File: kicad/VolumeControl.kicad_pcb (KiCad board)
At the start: 2 copper layers, 47 parts, among them P1 PWR_IN, P2 SOURCE_1, P3 SOURCE_2, P4 CONTROL, P5 AUDIO_OUT, P6 PWR_OUT, U1 ILQ74, U2 7805, U3 TMR_3-1221, U4 OPA1664, U5 PGA4311, U6 OPA1664

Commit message: Adding untracked files
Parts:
- removed C10, C11: 0.1u, Capacitors_SMD:C_1206_HandSoldering
- removed the REF** at (87.6, 124.5)
- removed the REF** at (87.6, 88.9)
- removed the REF** at (166.4, 88.9)
- removed the REF** at (166.4, 124.5)
- removed U6: OPA1664, SMD_Packages:SOIC-14_N
- added P7: AUDIO_OUT, JST:JST-4RA, F.Cu at (184.2, 87.6)
- added REF**: MountingHole_3.2mm_M3, Mounting_Holes:MountingHole_3.2mm_M3, F.Cu at (106.7, 86.4)
- added REF**: MountingHole_3.2mm_M3, Mounting_Holes:MountingHole_3.2mm_M3, F.Cu at (106.6, 123.3)
- added REF**: MountingHole_3.2mm_M3, Mounting_Holes:MountingHole_3.2mm_M3, F.Cu at (196.6, 123.3)
- added REF**: MountingHole_3.2mm_M3, Mounting_Holes:MountingHole_3.2mm_M3, F.Cu at (196.6, 86.3)
- C2: value 0.33u -> 0.1u
- C5: value 0.1u -> 1u
- C7: value 1u -> 0.1u
- P1: footprint Pin_Headers:Pin_Header_Straight_1x02 -> JST:JST-3RA
- P2: value SOURCE_1 -> PWR_OUT; footprint Pin_Headers:Pin_Header_Straight_1x04 -> JST:JST-2RA
- P3: value SOURCE_2 -> SOURCE_1; footprint Pin_Headers:Pin_Header_Straight_1x04 -> JST:JST-4RA
- P4: value CONTROL -> SOURCE_2; footprint Pin_Headers:Pin_Header_Straight_1x05 -> JST:JST-4RA
- P5: value AUDIO_OUT -> CONTROL; footprint Pin_Headers:Pin_Header_Straight_1x04 -> JST:JST-5RA
- P6: value PWR_OUT -> AUDIO_OUT; footprint Pin_Headers:Pin_Header_Straight_1x02 -> JST:JST-4RA
- U2: value 7805 -> TMR_3-1221; footprint Power_Integrations:TO-220 -> TracoPower:TMR_3
- U3: value TMR_3-1221 -> OPA1664; footprint TracoPower:TMR_3 -> SMD_Packages:SOIC-14_N
- U4: value OPA1664 -> PGA4311; footprint SMD_Packages:SOIC-14_N -> SMD_Packages:SOIC-28
- U5: value PGA4311 -> OPA1664; footprint SMD_Packages:SOIC-28 -> SMD_Packages:SOIC-14_N
- moved P6 96.7 mm to (184.2, 121.9)
- moved P4 84.2 mm to (170.2, 121.9), turned to 0 degrees
- moved C7 76.9 mm to (191.1, 108.6)
- moved C3 69.3 mm to (158.1, 87.6), turned to 180 degrees
- moved R13 58.5 mm to (172.7, 94.6), turned to 270 degrees
- moved U5 52.6 mm to (184.3, 109.2), turned to 270 degrees
- moved C4 49.6 mm to (165.7, 87.6), turned to 180 degrees
- moved P5 48.7 mm to (119.4, 121.9)
- moved R11 48.4 mm to (167.6, 116.8), turned to 0 degrees
- moved U3 44.1 mm to (163.2, 109.2), turned to 270 degrees
- moved C6 42.7 mm to (177.2, 108.6), turned to 90 degrees
- moved R12 41.9 mm to (172.7, 116.8)
- moved P3 40.9 mm to (156.2, 121.9), turned to 0 degrees
- moved R9 40.9 mm to (153.7, 116.8)
- moved U2 40.9 mm to (133.3, 102.2), turned to 0 degrees
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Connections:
- C2 pad 1: +12V -> +5VD
- C3 pad 1: +5VD -> +5VA
- C3 pad 2: GNDD -> GNDA
- C4 pad 1: +5VD -> GNDA
- C4 pad 2: GNDD -> -5VA
- C5 pad 1: +5VA -> +5VD
- C5 pad 2: GNDA -> GNDD
- C6 pad 1: GNDA -> +5VA
- C6 pad 2: -5VA -> GNDA
- C7 pad 1: +5VD -> GNDA
- C7 pad 2: GNDD -> -5VA
- P1 pad 1: +12V -> +5VD
- P1 pad 2: GNDD -> +12V
- P2 pad 1: /Audio Processing/SOURCE_1_LEFT -> +5VD
- P2 pad 2: GNDA -> GNDD
- P3 pad 1: /Audio Processing/SOURCE_2_LEFT -> /Audio Processing/SOURCE_1_LEFT
- P3 pad 2: GNDA -> GNDD
- P3 pad 3: GNDA -> GNDD
- P3 pad 4: /Audio Processing/SOURCE_2_RIGHT -> /Audio Processing/SOURCE_1_RIGHT
- P4 pad 1: /Digital Control/MUTE -> /Audio Processing/SOURCE_2_LEFT
- P4 pad 2: /Digital Control/CS -> GNDD
- P4 pad 3: /Digital Control/SDA -> GNDD
- P4 pad 4: /Digital Control/SCL -> /Audio Processing/SOURCE_2_RIGHT
- P5 pad 1: /Audio Processing/LEFT -> /Digital Control/MUTE
- P5 pad 2: GNDA -> /Digital Control/CS
- P5 pad 3: GNDA -> /Digital Control/SDA
- P5 pad 4: /Audio Processing/RIGHT -> /Digital Control/SCL
- P6 pad 1: +5VD -> /Audio Processing/LEFT
- P6 pad 2: GNDD -> GNDA
- R1 pad 2: /Digital Control/SCL -> /Digital Control/MUTE
- R10 pad 1: /Audio Processing/SOURCE_2_LEFT -> /Audio Processing/SOURCE_1_RIGHT
- R10 pad 2: GNDA -> GNDD
- R11 pad 1: /Audio Processing/SOURCE_1_RIGHT -> /Audio Processing/SOURCE_2_LEFT
- R11 pad 2: GNDA -> GNDD
- R12 pad 2: GNDA -> GNDD
- R2 pad 2: /Digital Control/SDA -> /Digital Control/CS
- R3 pad 2: /Digital Control/CS -> /Digital Control/SDA
- R4 pad 2: /Digital Control/MUTE -> /Digital Control/SCL
- R5 pad 1: /Audio Processing/SCL_ISOLATED -> /Audio Processing/MUTE_ISOLATED
- R6 pad 1: /Audio Processing/SDA_ISOLATED -> /Audio Processing/CS_ISOLATED
- R7 pad 1: /Audio Processing/CS_ISOLATED -> /Audio Processing/SDA_ISOLATED
- R8 pad 1: /Audio Processing/MUTE_ISOLATED -> /Audio Processing/SCL_ISOLATED
- R9 pad 2: GNDA -> GNDD
- U1 pad 10: /Audio Processing/MUTE_ISOLATED -> /Audio Processing/SCL_ISOLATED
- U1 pad 11: /Audio Processing/CS_ISOLATED -> /Audio Processing/SDA_ISOLATED
- U1 pad 14: /Audio Processing/SDA_ISOLATED -> /Audio Processing/CS_ISOLATED
- U1 pad 15: /Audio Processing/SCL_ISOLATED -> /Audio Processing/MUTE_ISOLATED
- U2 pad 1: +12V -> GNDD
- U2 pad 2: GNDD -> Net-(L1-Pad2)
- U2 pad 3: +5VD -> Net-(U2-Pad3)
- U3 pad 1: GNDD -> Net-(U3-Pad1)
- U3 pad 2: Net-(L1-Pad2) -> Net-(U3-Pad1)
- U3 pad 3: Net-(U3-Pad3) -> /Audio Processing/SOURCE_1_LEFT
- U3 pad 5: Net-(U3-Pad5) -> /Audio Processing/SOURCE_1_RIGHT
- U3 pad 6: +5VA -> Net-(U3-Pad6)
- U3 pad 7: GNDA -> Net-(U3-Pad6)
- U3 pad 8: -5VA -> Net-(U3-Pad8)
- U4 pad 1: Net-(U4-Pad1) -> /Audio Processing/MUTE_ISOLATED
- U4 pad 10: /Audio Processing/SOURCE_1_RIGHT -> Net-(U3-Pad1)
- U4 pad 11: -5VA -> GNDA
- U4 pad 12: /Audio Processing/SOURCE_2_RIGHT -> +5VD
- U4 pad 13: Net-(U4-Pad13) -> /Audio Processing/SDA_ISOLATED
- U4 pad 14: Net-(U4-Pad13) -> /Audio Processing/CS_ISOLATED
- U4 pad 2: Net-(U4-Pad1) -> GNDA
- U4 pad 3: /Audio Processing/SOURCE_1_LEFT -> Net-(U3-Pad8)
- U4 pad 4: +5VA -> GNDA
- U4 pad 5: /Audio Processing/SOURCE_2_LEFT -> Net-(R14-Pad2)
- U4 pad 6: Net-(U4-Pad6) -> -5VA
- U4 pad 7: Net-(U4-Pad6) -> +5VA
- U4 pad 8: Net-(U4-Pad8) -> Net-(R15-Pad2)
- U4 pad 9: Net-(U4-Pad8) -> GNDA
- U5 pad 1: /Audio Processing/MUTE_ISOLATED -> /Audio Processing/LEFT
- U5 pad 10: Net-(U4-Pad8) -> (no net)
- U5 pad 11: GNDA -> -5VA
- U5 pad 12: +5VD -> GNDA
- U5 pad 13: /Audio Processing/SDA_ISOLATED -> Net-(R16-Pad1)
- U5 pad 14: /Audio Processing/CS_ISOLATED -> /Audio Processing/RIGHT
- U5 pad 2: GNDA -> Net-(R14-Pad1)
- U5 pad 3: Net-(U4-Pad1) -> GNDA
- U5 pad 4: GNDA -> +5VA
- U5 pad 5: Net-(R14-Pad2) -> (no net)
- U5 pad 6: -5VA -> (no net)
- U5 pad 7: +5VA -> (no net)
- U5 pad 8: Net-(R16-Pad2) -> (no net)
- U5 pad 9: GNDA -> (no net)
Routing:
- net GNDA: track 0.00 -> 84.9 mm, vias 0 -> 2
- net /Audio Processing/MUTE_ISOLATED: track 0.00 -> 78.8 mm, vias 0 -> 2
- net +5VD: track 0.00 -> 61.5 mm, vias 0 -> 2
- net /Audio Processing/CS_ISOLATED: track 0.00 -> 51.2 mm, vias 0 -> 1
- net /Audio Processing/SDA_ISOLATED: track 0.00 -> 45.3 mm, vias 0 -> 1
- net GNDD: track 0.00 -> 43.7 mm, vias 0 -> 1
- net /Audio Processing/RIGHT: track 0.00 -> 41.1 mm
- net /Audio Processing/LEFT: track 0.00 -> 39.8 mm, vias 0 -> 2
- net +5VA: track 0.00 -> 39.8 mm, vias 0 -> 2
- net /Audio Processing/SCL_ISOLATED: track 0.00 -> 38.1 mm, vias 0 -> 1
- net Net-(R17-Pad2): track 0.00 -> 30.4 mm, vias 0 -> 2
- net /Digital Control/CTRL_GND: track 0.00 -> 29.2 mm
- net Net-(R15-Pad2): track 0.00 -> 26.8 mm, vias 0 -> 5
- net Net-(R16-Pad2): track 0.00 -> 25.4 mm, vias 0 -> 2
- net Net-(U3-Pad8): track 0.00 -> 24.7 mm, vias 0 -> 2
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- added copper zone on In2.Cu, net +5VA
- added copper zone on In2.Cu, net +5VD
- added copper zone on In2.Cu, net -5VA
- added copper zone on In1.Cu, net GNDA
- added copper zone on In1.Cu, net GNDD
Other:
- board outline added: 100 x 47 mm
- copper layers 2 -> 4
- net class Default: trace_width 0.25 -> 0.5
- net class Power added: clearance 0.2, trace_width 1, via_dia 1, via_drill 0.6
- rule pad_to_mask_clearance: 0.2 -> 0
- board text added: "5V OUT"
- board text added: "AUDIO_OUT"
- board text added: "CONTROL"
- board text added: "POWER"
- board text added: "SOURCE_1"
- board text added: "SOURCE_2"
- board text added: "Volume Control V1.0"
- board text added: "v@nce.me"

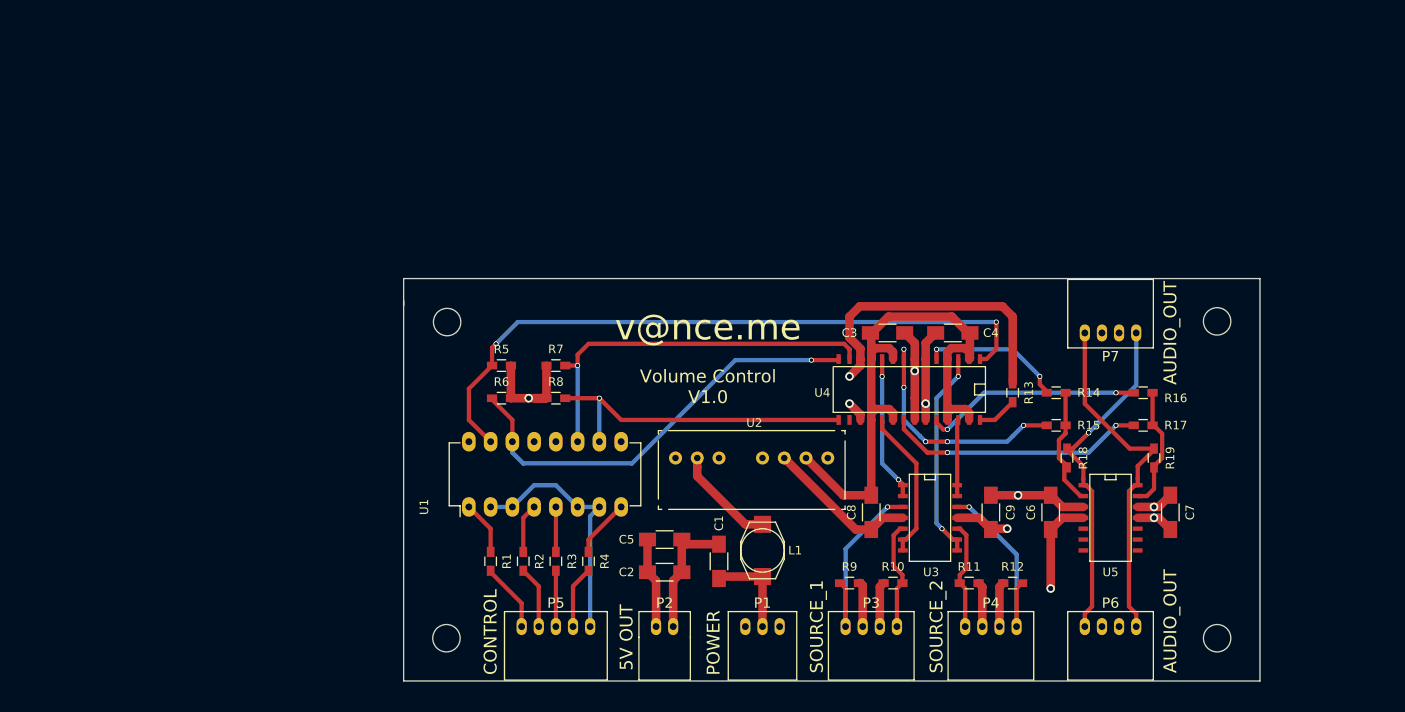
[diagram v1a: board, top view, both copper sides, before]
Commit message: Routed the board.  Passes ERC check
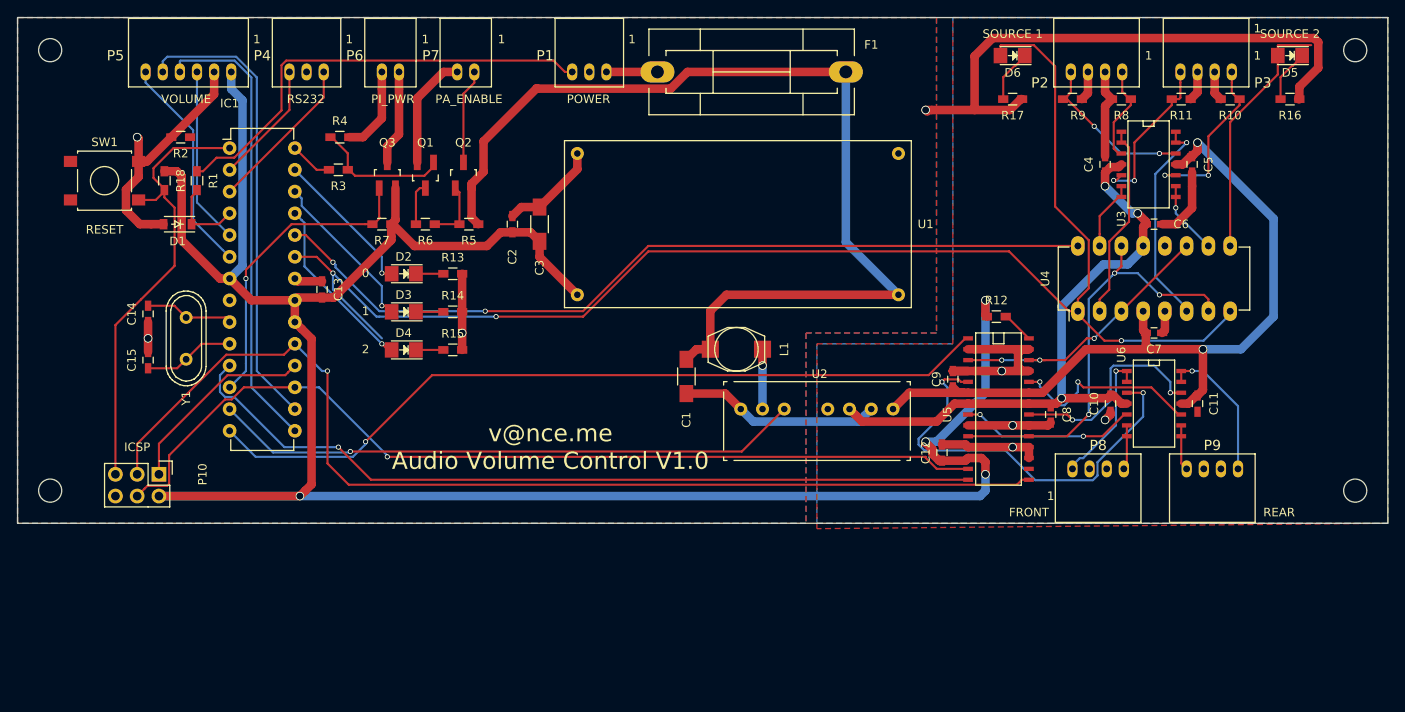
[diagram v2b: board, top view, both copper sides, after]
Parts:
- removed R19: 47k, Resistors_SMD:R_0603_HandSoldering
- removed the REF** at (106.7, 86.4)
- removed the REF** at (106.6, 123.3)
- removed the REF** at (196.6, 123.3)
- removed the REF** at (196.6, 86.3)
- added C10: 0.1u, Capacitors_SMD:C_0603_HandSoldering, F.Cu at (184.2, 95.9)
- added C11: 0.1u, Capacitors_SMD:C_0603_HandSoldering, F.Cu at (194.3, 95.9)
- added C12: 0.1u, Capacitors_SMD:C_0603_HandSoldering, F.Cu at (164.5, 101.6)
- added C13: 0.1u, Capacitors_SMD:C_0603_HandSoldering, F.Cu at (92.1, 82.5)
- added C14: 22p, Capacitors_SMD:C_0603_HandSoldering, F.Cu at (71.8, 85.4)
- added C15: 22p, Capacitors_SMD:C_0603_HandSoldering, F.Cu at (71.8, 90.8)
- added D1: 5.1V, Diodes_SMD:SOD-123, F.Cu at (75.2, 74.9)
- added D2: 0, LEDs:LED_1206, F.Cu at (101.6, 80.7)
- added D3: 1, LEDs:LED_1206, F.Cu at (101.6, 85.2)
- added D4: 2, LEDs:LED_1206, F.Cu at (101.6, 89.6)
- added D5: S2, LEDs:LED_1206, F.Cu at (205.1, 55.2)
- added D6: S1, LEDs:LED_1206, F.Cu at (172.7, 55.2)
- added F1: 1A, Fuse_Holders_and_Fuses:Fuseholder5x20_horiz_SemiClosed_Casing10x25mm, F.Cu at (142.2, 57.1)
- added IC1: ATMEGA328P-P, Housings_DIP:DIP-28_W7.62mm, F.Cu at (81.3, 66.0)
- added P10: ICSP, Pin_Headers:Pin_Header_Straight_2x03, F.Cu at (73.0, 104.1)
- added P8: FRONT, JST:JST-4RA, F.Cu at (182.7, 103.5)
- added P9: REAR, JST:JST-4RA, F.Cu at (196.0, 103.5)
- added Q1: BC848B, TO_SOT_Packages_SMD:SOT-23_Handsoldering, F.Cu at (104.1, 69.2)
- added Q2: Si2301BDS, TO_SOT_Packages_SMD:SOT-23_Handsoldering, F.Cu at (108.6, 69.2)
- added Q3: Si2301BDS, TO_SOT_Packages_SMD:SOT-23_Handsoldering, F.Cu at (99.7, 69.2)
- added REF**: MountingHole_2.7mm_M2.5_ISO7380, Mounting_Holes:MountingHole_2.7mm_M2.5_ISO7380, F.Cu at (212.7, 54.6)
- added REF**: MountingHole_2.7mm_M2.5_ISO7380, Mounting_Holes:MountingHole_2.7mm_M2.5_ISO7380, F.Cu at (60.3, 54.6)
- added REF**: MountingHole_2.7mm_M2.5_ISO7380, Mounting_Holes:MountingHole_2.7mm_M2.5_ISO7380, F.Cu at (212.7, 106.0)
- added REF**: MountingHole_2.7mm_M2.5_ISO7380, Mounting_Holes:MountingHole_2.7mm_M2.5_ISO7380, F.Cu at (60.3, 106.0)
- added SW1: SW_PUSH, Buttons_Switches_SMD:SW_SPST_B3S-1000, F.Cu at (66.7, 69.8)
- added U6: OPA1664, SMD_Packages:SOIC-14_N, F.Cu at (189.4, 95.9)
- added Y1: 16MHz, Crystals:Crystal_HC49-U_Vertical, F.Cu at (76.2, 88.3)
- C2, C4, C6, C7, C8, C9: footprint Capacitors_SMD:C_1206_HandSoldering -> Capacitors_SMD:C_0603_HandSoldering
- C3: value 0.1u -> 1u
- C5: value 1u -> 0.1u; footprint Capacitors_SMD:C_1206_HandSoldering -> Capacitors_SMD:C_0603_HandSoldering
- P2: value PWR_OUT -> SOURCE_1; footprint JST:JST-2RA -> JST:JST-4RA
- P3: value SOURCE_1 -> SOURCE_2
- P4: value SOURCE_2 -> RS232; footprint JST:JST-4RA -> JST:JST-3RA
- P5: value CONTROL -> VOL_KNOB; footprint JST:JST-5RA -> JST:JST-6RA
- P6: value AUDIO_OUT -> PI_PWR; footprint JST:JST-4RA -> JST:JST-2RA
- P7: value AUDIO_OUT -> PA_EN; footprint JST:JST-4RA -> JST:JST-2RA
- R1, R3, R4: value 200 -> 10k
- R13, R14, R15, R16, R17: value 47k -> 220
- R18, R5, R7: value 47k -> 10k
- R2: value 200 -> 22k
- R6: value 47k -> 22k
- U1: value ILQ74 -> Buck_Converter; footprint Housings_DIP:DIP-16_W7.62mm_LongPads -> Buck_Converter:Buck_Converter
- U4: value PGA4311 -> DG308; footprint SMD_Packages:SOIC-28 -> Housings_DIP:DIP-16_W7.62mm_LongPads
- U5: value OPA1664 -> PGA4311; footprint SMD_Packages:SOIC-14_N -> SMD_Packages:SOIC-28
- moved R18 110.3 mm to (73.7, 69.8)
- moved P6 106.1 mm to (100.1, 57.1), turned to 180 degrees
- moved P4 102.9 mm to (90.3, 57.1), turned to 180 degrees
- moved P2 82.1 mm to (182.5, 57.1), turned to 180 degrees
- moved P7 81.2 mm to (108.9, 57.1)
- moved P5 77.7 mm to (76.5, 57.1), turned to 180 degrees
- moved P3 75.7 mm to (195.3, 57.1), turned to 180 degrees
- moved C5 75.6 mm to (193.7, 67.9), turned to 90 degrees
- moved R8 74.7 mm to (185.4, 60.3)
- moved R14 71.1 mm to (107.3, 85.2), turned to 0 degrees
- moved R15 71.0 mm to (107.3, 89.6), turned to 0 degrees
- moved R10 68.9 mm to (198.1, 60.3)
- moved P1 67.9 mm to (123.3, 57.1), turned to 180 degrees
- moved R13 66.8 mm to (107.3, 80.7), turned to 0 degrees
- moved R2 63.7 mm to (75.6, 64.8), turned to 180 degrees
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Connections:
- C1 pad 1: +12V -> Net-(C1-Pad1)
- C1 pad 2: GNDD -> GND
- C2 pad 2: GNDD -> GND
- C3 pad 1: +5VA -> +5VD
- C3 pad 2: GNDA -> GND
- C4 pad 1: GNDA -> +5VA
- C4 pad 2: -5VA -> GND
- C5 pad 1: +5VD -> GND
- C5 pad 2: GNDD -> -5VA
- C6 pad 2: GNDA -> GND
- C7 pad 1: GNDA -> GND
- C8 pad 2: GNDA -> GND
- C9 pad 1: GNDA -> GND
- L1 pad 1: +12V -> Net-(C1-Pad1)
- P1 pad 1: +5VD -> /Power/+12V_SUPPLY
- P1 pad 2: +12V -> GND
- P1 pad 3: GNDD -> /Power/+12V_IGNITION
- P2 pad 1: +5VD -> /Audio Processing/SOURCE_1_LEFT
- P2 pad 2: GNDD -> GND
- P3 pad 1: /Audio Processing/SOURCE_1_LEFT -> /Audio Processing/SOURCE_2_LEFT
- P3 pad 2: GNDD -> GND
- P3 pad 3: GNDD -> GND
- P3 pad 4: /Audio Processing/SOURCE_1_RIGHT -> /Audio Processing/SOURCE_2_RIGHT
- P4 pad 1: /Audio Processing/SOURCE_2_LEFT -> /DIgital_Control/TX_OUT
- P4 pad 2: GNDD -> GND
- P4 pad 3: GNDD -> /DIgital_Control/RX_IN
- P5 pad 1: /Digital Control/MUTE -> +5VD
- P5 pad 2: /Digital Control/CS -> GND
- P5 pad 3: /Digital Control/SDA -> /DIgital_Control/BTN
- P5 pad 4: /Digital Control/SCL -> /DIgital_Control/ROT_A
- P5 pad 5: /Digital Control/CTRL_GND -> /DIgital_Control/ROT_B
- P6 pad 1: /Audio Processing/LEFT -> /Power/+5V_PI
- P6 pad 2: GNDA -> GND
- P7 pad 1: /Audio Processing/LEFT -> /Power/+12V_PA_ENABLE
- P7 pad 2: GNDA -> GND
- R1 pad 1: Net-(R1-Pad1) -> /Power/+12V_IGNITION
- R1 pad 2: /Digital Control/MUTE -> /DIgital_Control/IGNITION
- R10 pad 1: /Audio Processing/SOURCE_1_RIGHT -> /Audio Processing/SOURCE_2_LEFT
- R10 pad 2: GNDD -> GND
- R11 pad 1: /Audio Processing/SOURCE_2_LEFT -> /Audio Processing/SOURCE_2_RIGHT
- R11 pad 2: GNDD -> GND
- R12 pad 1: /Audio Processing/SOURCE_2_RIGHT -> +5VD
- R12 pad 2: GNDD -> Net-(R12-Pad2)
- R13 pad 1: +5VD -> Net-(D2-Pad1)
- R13 pad 2: Net-(R13-Pad2) -> GND
- R14 pad 1: Net-(R14-Pad1) -> Net-(D3-Pad1)
- R14 pad 2: Net-(R14-Pad2) -> GND
- R15 pad 1: Net-(R14-Pad1) -> Net-(D4-Pad1)
- R15 pad 2: Net-(R15-Pad2) -> GND
- R16 pad 1: Net-(R16-Pad1) -> Net-(D5-Pad1)
- R16 pad 2: Net-(R16-Pad2) -> GND
- R17 pad 1: Net-(R16-Pad1) -> Net-(D6-Pad1)
- R17 pad 2: Net-(R17-Pad2) -> GND
- R18 pad 1: /Audio Processing/LEFT -> +5VD
- R18 pad 2: Net-(R14-Pad1) -> /DIgital_Control/RESET
- R2 pad 1: Net-(R2-Pad1) -> /DIgital_Control/IGNITION
- R2 pad 2: /Digital Control/CS -> GND
- R3 pad 1: Net-(R3-Pad1) -> Net-(Q1-Pad1)
- R3 pad 2: /Digital Control/SDA -> /DIgital_Control/PA_ENABLE
- R4 pad 1: Net-(R4-Pad1) -> Net-(Q1-Pad1)
- R4 pad 2: /Digital Control/SCL -> GND
- R5 pad 1: /Audio Processing/MUTE_ISOLATED -> Net-(C1-Pad1)
- R5 pad 2: +5VD -> Net-(Q2-Pad1)
- R6 pad 1: /Audio Processing/CS_ISOLATED -> Net-(Q2-Pad1)
- R6 pad 2: +5VD -> Net-(Q1-Pad3)
- R7 pad 1: /Audio Processing/SDA_ISOLATED -> /DIgital_Control/PI_ENABLE
- R8 pad 1: /Audio Processing/SCL_ISOLATED -> /Audio Processing/SOURCE_1_LEFT
- R8 pad 2: +5VD -> GND
- R9 pad 1: /Audio Processing/SOURCE_1_LEFT -> /Audio Processing/SOURCE_1_RIGHT
- R9 pad 2: GNDD -> GND
- U1 pad 1: Net-(R1-Pad1) -> Net-(C1-Pad1)
- U1 pad 2: /Digital Control/CTRL_GND -> GND
- U1 pad 3: /Digital Control/CTRL_GND -> +5VD
- U1 pad 4: Net-(R2-Pad1) -> GND
- U2 pad 1: GNDD -> GND
- U2 pad 3: Net-(U2-Pad3) -> /DIgital_Control/AUDIO_ENABLE
- U2 pad 7: GNDA -> GND
- U3 pad 12: /Audio Processing/SOURCE_2_RIGHT -> /Audio Processing/SOURCE_1_RIGHT
- U3 pad 5: /Audio Processing/SOURCE_1_RIGHT -> /Audio Processing/SOURCE_2_RIGHT
- U4 pad 1: /Audio Processing/MUTE_ISOLATED -> /Audio Processing/SOURCE_1_ENABLE
- U4 pad 10: Net-(U3-Pad1) -> Net-(U3-Pad8)
- U4 pad 11: GNDA -> Net-(U4-Pad11)
- U4 pad 12: +5VD -> (no net)
- U4 pad 13: /Audio Processing/SDA_ISOLATED -> +5VA
- U4 pad 14: /Audio Processing/CS_ISOLATED -> Net-(U4-Pad14)
- U4 pad 15: /Audio Processing/SCL_ISOLATED -> Net-(U3-Pad6)
- U4 pad 16: Net-(U4-Pad16) -> /Audio Processing/SOURCE_2_ENABLE
- U4 pad 2: GNDA -> Net-(U3-Pad1)
- U4 pad 3: Net-(U3-Pad8) -> Net-(U4-Pad11)
- U4 pad 4: GNDA -> -5VA
- U4 pad 5: Net-(R14-Pad2) -> GND
- U4 pad 6: -5VA -> Net-(U3-Pad13)
- U4 pad 7: +5VA -> Net-(U4-Pad14)
- U4 pad 8: Net-(R15-Pad2) -> /Audio Processing/SOURCE_1_ENABLE
- U4 pad 9: GNDA -> /Audio Processing/SOURCE_2_ENABLE
- U5 pad 1: /Audio Processing/LEFT -> /Audio Processing/MUTE
- U5 pad 10: (no net) -> Net-(U4-Pad14)
- U5 pad 11: -5VA -> GND
- U5 pad 12: GNDA -> +5VD
- U5 pad 13: Net-(R16-Pad1) -> /Audio Processing/SDI
- U5 pad 14: /Audio Processing/RIGHT -> /Audio Processing/CS
- U5 pad 2: Net-(R14-Pad1) -> GND
- U5 pad 3: GNDA -> Net-(U4-Pad11)
- U5 pad 4: +5VA -> GND
- U5 pad 5: (no net) -> Net-(U5-Pad5)
- U5 pad 6: (no net) -> -5VA
- U5 pad 7: (no net) -> +5VA
- U5 pad 8: (no net) -> Net-(U5-Pad8)
- U5 pad 9: (no net) -> GND
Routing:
- net GND: track 0.00 -> 247.6 mm, vias 0 -> 8
- net +5VD: track 61.5 -> 270.7 mm, vias 2 -> 4
- net /Audio Processing/SOURCE_1_ENABLE: track 0.00 -> 170.7 mm, vias 0 -> 3
- net /Audio Processing/SOURCE_2_ENABLE: track 0.00 -> 128.1 mm, vias 0 -> 2
- net /Audio Processing/SCLK: track 0.00 -> 125.9 mm, vias 0 -> 1
- net Net-(C1-Pad1): track 0.00 -> 115.4 mm
- net /Audio Processing/SDI: track 0.00 -> 108.7 mm, vias 0 -> 1
- net /Audio Processing/CS: track 0.00 -> 95.2 mm, vias 0 -> 1
- net /Audio Processing/MUTE: track 0.00 -> 93.4 mm, vias 0 -> 1
- net GNDA: track 84.9 -> 0.00 mm, vias 2 -> 0
- net /Audio Processing/MUTE_ISOLATED: track 78.8 -> 0.00 mm, vias 2 -> 0
- net -5VA: track 21.5 -> 91.4 mm, vias 3 -> 2
- net /DIgital_Control/AUDIO_ENABLE: track 0.00 -> 69.0 mm, vias 0 -> 1
- net /DIgital_Control/ROT_B: track 0.00 -> 54.0 mm
- net /DIgital_Control/ROT_A: track 0.00 -> 53.8 mm
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- added copper zone on B.Cu, net GND
- added copper zone on F.Cu, net GND
- removed copper zone on In2.Cu, net +5VA
- removed copper zone on In2.Cu, net +5VD
- removed copper zone on In2.Cu, net -5VA
- removed copper zone on In1.Cu, net GNDA
- removed copper zone on In1.Cu, net GNDD
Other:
- board size 100 x 47 mm -> 160 x 59.1 mm
- copper layers 4 -> 2
- net class Default: trace_width 0.5 -> 0.25
- net class Power: via_drill 0.6 -> 0.8
- board text added: "0"
- board text added: "1"
- board text added: "2"
- board text added: "FRONT"
- board text added: "ICSP"
- board text added: "PA_ENABLE"
- board text added: "PI_PWR"
- board text added: "REAR"
- board text added: "RESET"
- board text added: "RS232"
- board text added: "SOURCE 1"
- board text added: "SOURCE 2"
- board text added: "VOLUME"
- board text added: "v@nce.me Audio Volume Control V1.0"
- board text removed: "5V OUT"
- board text removed: "AUDIO_OUT"
- board text removed: "CONTROL"
- board text removed: "SOURCE_1"
- board text removed: "SOURCE_2"
- board text removed: "Volume Control V1.0"
- board text removed: "v@nce.me"

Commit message: Minor change
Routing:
- net GND: track 247.6 -> 241.6 mm, vias 8 -> 7
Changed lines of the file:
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@@
     (thickness 1.6)
     (drawings 32)
-    (tracks 649)
+    (tracks 645)
     (zones 0)
     (modules 67)
@@
   (segment (start 177.165 98.105) (end 176.845 98.425) (width 1) (layer F.Cu) (net 2))
   (segment (start 176.845 98.425) (end 174.625 98.425) (width 1) (layer F.Cu) (net 2))
-  (segment (start 168.275 61.595) (end 163.267106 61.595) (width 1) (layer F.Cu) (net 2))
   (segment (start 172.4 61.595) (end 168.275 61.595) (width 1) (layer F.Cu) (net 2))
   (segment (start 206.205 58.875) (end 206.205 60.325) (width 1) (layer F.Cu) (net 2))
@@
   (segment (start 173.82 60.325) (end 173.67 60.325) (width 1) (layer F.Cu) (net 2))
   (segment (start 173.67 60.325) (end 172.4 61.595) (width 1) (layer F.Cu) (net 2))
-  (segment (start 163.267106 61.595) (end 162.56 61.595) (width 1) (layer F.Cu) (net 2))
   (segment (start 196.31 57.15) (end 196.31 59.615) (width 1) (layer F.Cu) (net 2))
   (segment (start 196.31 59.615) (end 197.02 60.325) (width 1) (layer F.Cu) (net 2))
@@
   (segment (start 194.31 59.52) (end 194.31 57.15) (width 1) (layer F.Cu) (net 2))
   (segment (start 206.205 60.325) (end 206.055 60.325) (width 1) (layer F.Cu) (net 2))
-  (segment (start 162.74 61.775) (end 162.56 61.595) (width 1) (layer F.Cu) (net 2))
-  (via (at 162.56 61.595) (size 1) (drill 0.8) (layers F.Cu B.Cu) (net 2))
   (segment (start 183.515 57.15) (end 183.515 59.52) (width 1) (layer F.Cu) (net 2))
   (segment (start 183.515 59.52) (end 184.32 60.325) (width 1) (layer F.Cu) (net 2))
